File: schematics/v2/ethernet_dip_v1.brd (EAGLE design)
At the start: 41 x 50 mm, 30 parts

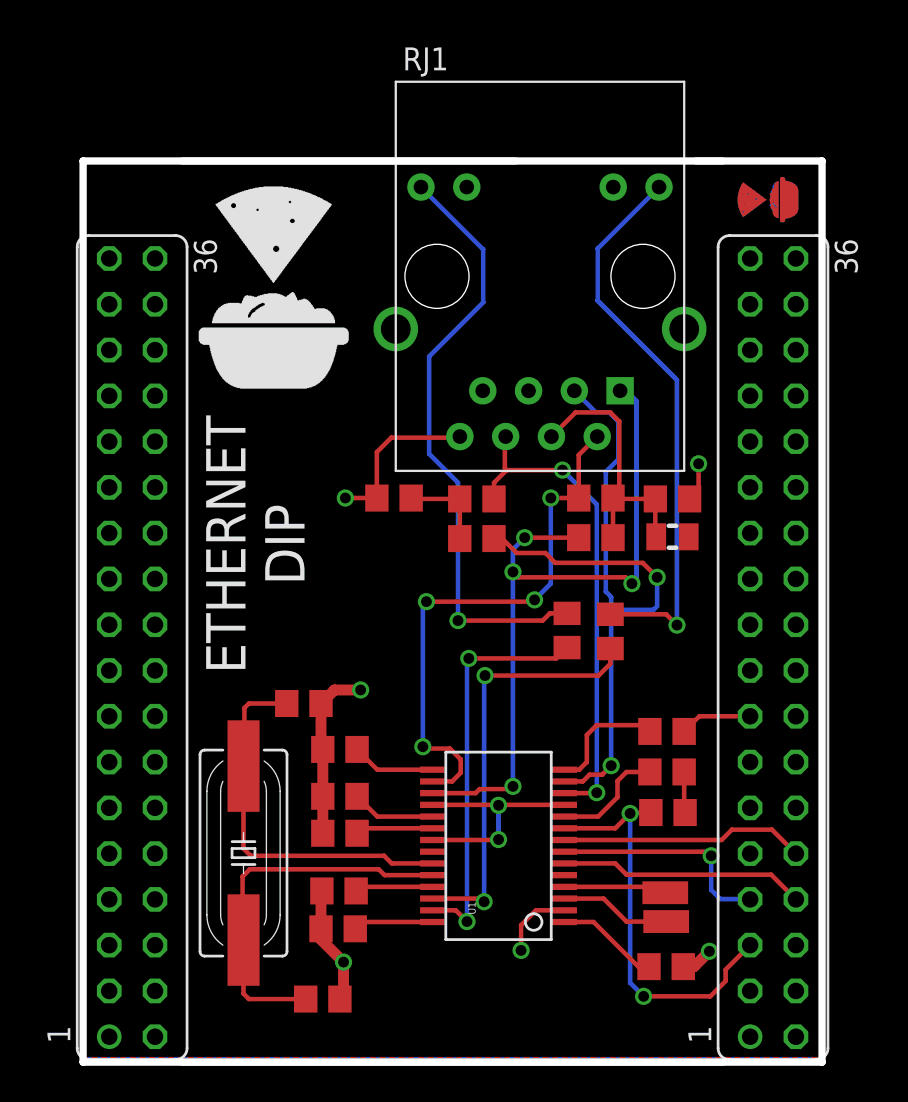
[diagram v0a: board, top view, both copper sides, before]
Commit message: added eeprom
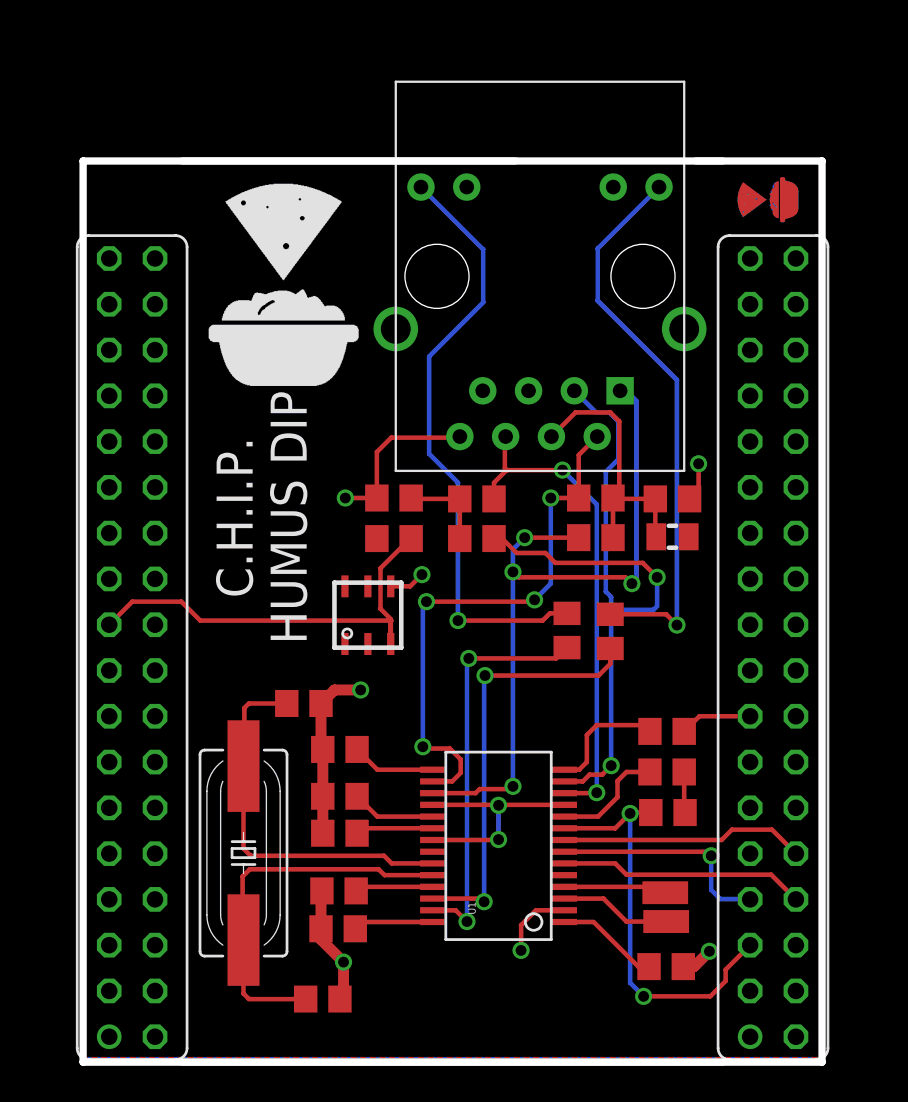
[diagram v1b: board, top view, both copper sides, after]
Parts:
- added IC2: DS2432P, 1wire:TSOC6
- added R10: (no value), rcl:R0805
- moved U$5 0.57 mm to (6.95, 37.5)
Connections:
- net GND: now also IC2.4
- net LD2: now also IC2.3, R10.1
- net VDD: now also R10.2
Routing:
- net LD2: track 0.00 -> 24.7 mm
- net GND: track 50.6 -> 52.6 mm, vias 8 -> 9
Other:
- board text added: "C.H.I.P. HUMUS DIP"
- board text removed: "ETHERNET DIP"
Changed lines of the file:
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@@
 <wire x1="0" y1="50" x2="0" y2="0" width="0.4064" layer="20"/>
 <wire x1="0" y1="0" x2="41" y2="0" width="0.4064" layer="20"/>
-<text x="9.5558" y="28.7165" size="2.1844" layer="25" font="vector" ratio="12" rot="R90" align="center">ETHERNET
-DIP </text>
+<text x="9.9058" y="30.2165" size="2" layer="25" font="vector" ratio="13" rot="R90" align="center">C.H.I.P.
+HUMUS DIP </text>
 <text x="5.7049" y="49.2006" size="1.27" layer="22" font="vector" ratio="12" rot="MR0" align="top-left"> JKW
 v0.1</text>
@@
 <element name="U$4" library="logo" package="LOGO_3X3_COPPER" value="LOGO_3X3_COPPER" x="38" y="47.85" rot="MR270"/>
 <element name="U$2" library="logo" package="LOGO_3X3_COPPER" value="LOGO_3X3_COPPER" x="38" y="47.85" rot="R90"/>
-<element name="U$5" library="logo" package="LOGO_10X10_SILK" value="LOGO_10X10_SILK" x="6.4" y="37.35"/>
+<element name="U$5" library="logo" package="LOGO_10X10_SILK" value="LOGO_10X10_SILK" x="6.95" y="37.5"/>
 <element name="U1" library="SparkFun-DigitalIC" package="SSOP28DB" value="" x="23.05" y="12" rot="R90"/>
-<element name="RJ1" library="CONNECTER" package="HR911105A" value="HR911105A" x="25.35" y="43.6" rot="R90"/>
+<element name="RJ1" library="CONNECTER" package="HR911105A" value="HR911105A" x="25.35" y="43.6" smashed="yes" rot="R90">
+<attribute name="VALUE" x="26.32" y="38.985" size="1.27" layer="27" rot="R90"/>
+</element>
 <element name="R1" library="rcl" package="R0805" value="2K" x="32.4" y="18.35" smashed="yes" rot="R180"/>
 <element name="C1" library="rcl" package="C0805" value="" x="32.35" y="5.3" smashed="yes">
@@
 <element name="R9" library="rcl" package="R0805" value="" x="29.25" y="23.9" smashed="yes" rot="R270">
 <attribute name="VALUE" x="26.71" y="24.535" size="1.27" layer="27" rot="R270"/>
+</element>
+<element name="IC2" library="1wire" package="TSOC6" value="DS2432P" x="15.8" y="24.8" smashed="yes"/>
+<element name="R10" library="rcl" package="R0805" value="" x="17.25" y="29.05" smashed="yes" rot="R180">
+<attribute name="VALUE" x="17.885" y="31.59" size="1.27" layer="27" rot="R180"/>
 </element>
 </elements>
@@
 <wire x1="33.65" y1="31.25" x2="34.15" y2="31.75" width="0.254" layer="1"/>
 <wire x1="34.15" y1="31.75" x2="34.15" y2="33.2" width="0.254" layer="1"/>
+<contactref element="IC2" pad="4"/>
+<contactref element="IC2" pad="4"/>
+<via x="18.8" y="27.05" extent="1-16" drill="0.6"/>
+<wire x1="17.07" y1="26.4002" x2="18.1502" y2="26.4002" width="0.254" layer="1"/>
+<wire x1="18.1502" y1="26.4002" x2="18.8" y2="27.05" width="0.254" layer="1"/>
 </signal>
 <signal name="INT0">
@@
 <signal name="LD2">
 <contactref element="SV2" pad="19"/>
+<contactref element="IC2" pad="3"/>
+<contactref element="R10" pad="1"/>
+<wire x1="17.07" y1="23.1998" x2="17.07" y2="24.58" width="0.254" layer="1"/>
+<wire x1="17.07" y1="24.58" x2="16.5" y2="25.15" width="0.254" layer="1"/>
+<wire x1="17.07" y1="23.1998" x2="17.07" y2="24.47" width="0.254" layer="1"/>
+<wire x1="17.07" y1="24.47" x2="17.1" y2="24.5" width="0.254" layer="1"/>
+<wire x1="17.1" y1="24.5" x2="6.5" y2="24.5" width="0.254" layer="1"/>
+<wire x1="16.5" y1="25.15" x2="16.5" y2="27.4" width="0.254" layer="1"/>
+<wire x1="16.5" y1="27.4" x2="18" y2="28.9" width="0.254" layer="1"/>
+<wire x1="18" y1="28.9" x2="18.2" y2="29.05" width="0.254" layer="1"/>
+<wire x1="6.5" y1="24.5" x2="5.45" y2="25.55" width="0.254" layer="1"/>
+<wire x1="5.45" y1="25.55" x2="2.73" y2="25.55" width="0.254" layer="1"/>
+<wire x1="2.73" y1="25.55" x2="1.45" y2="24.27" width="0.254" layer="1"/>
 </signal>
 <signal name="LD4">
@@
 <vertex x="0" y="10.47"/>
 </polygon>
+<contactref element="R10" pad="2"/>
 </signal>
 <signal name="N$2">

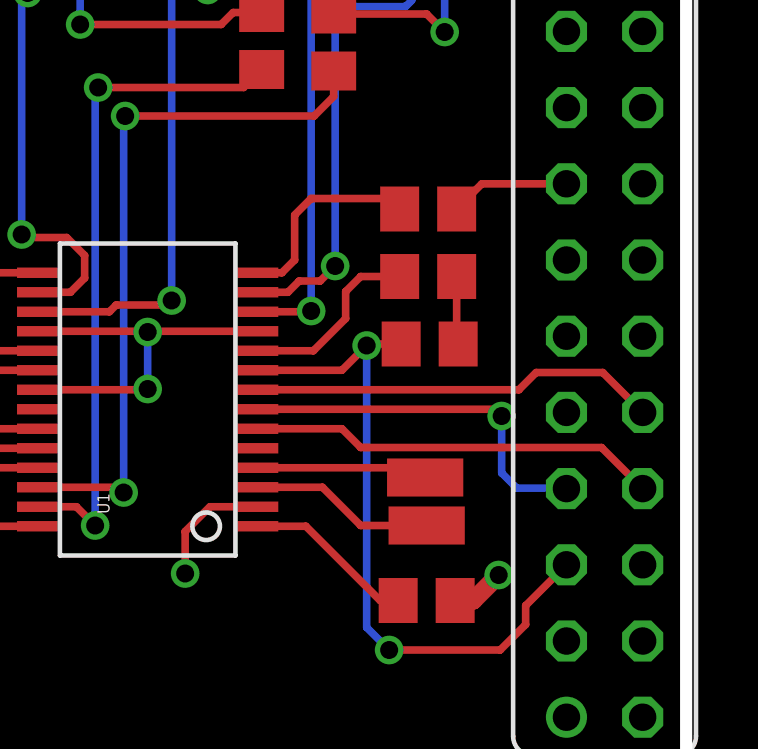
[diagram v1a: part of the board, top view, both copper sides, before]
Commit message: routed interrupt pin
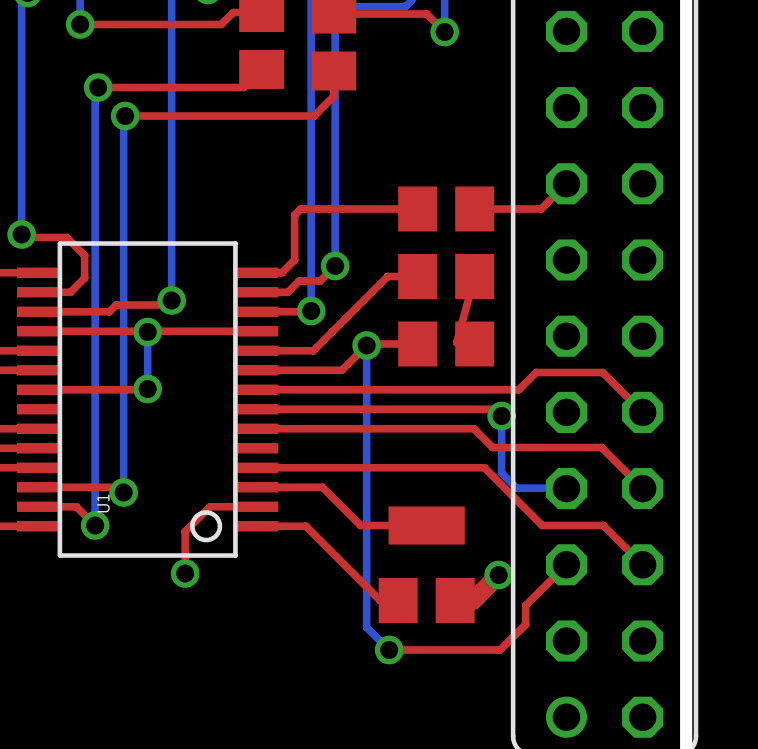
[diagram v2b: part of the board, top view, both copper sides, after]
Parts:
- removed PAD1: WIREPADSMD1,27-254, wirepad:SMD1,27-2,54
- moved R1 0.60 mm to (33.0, 18.4)
- moved R2 0.60 mm to (33.0, 16.1)
- moved R3 0.55 mm to (33.0, 13.8)
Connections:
- removed net N$12: PAD1.1, U1.4
- net D1: now also U1.4
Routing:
- net D1: track 0.00 -> 14.2 mm
- net N$12: track 5.73 -> 0.00 mm
- net VDD: track 24.7 -> 25.3 mm
- net GND: track 52.6 -> 52.0 mm
- net D0: track 23.1 -> 23.6 mm
